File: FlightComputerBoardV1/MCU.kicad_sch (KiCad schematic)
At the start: 42 parts, among them J16 USB_C_Receptacle_USB2.0_16P, J17 Conn_ST_STDC14, SW1 SW_Push, SW2 SW_Push, U20 STM32H723ZGTx, X1 NX3215SA-32.768K-STD-MUA-9

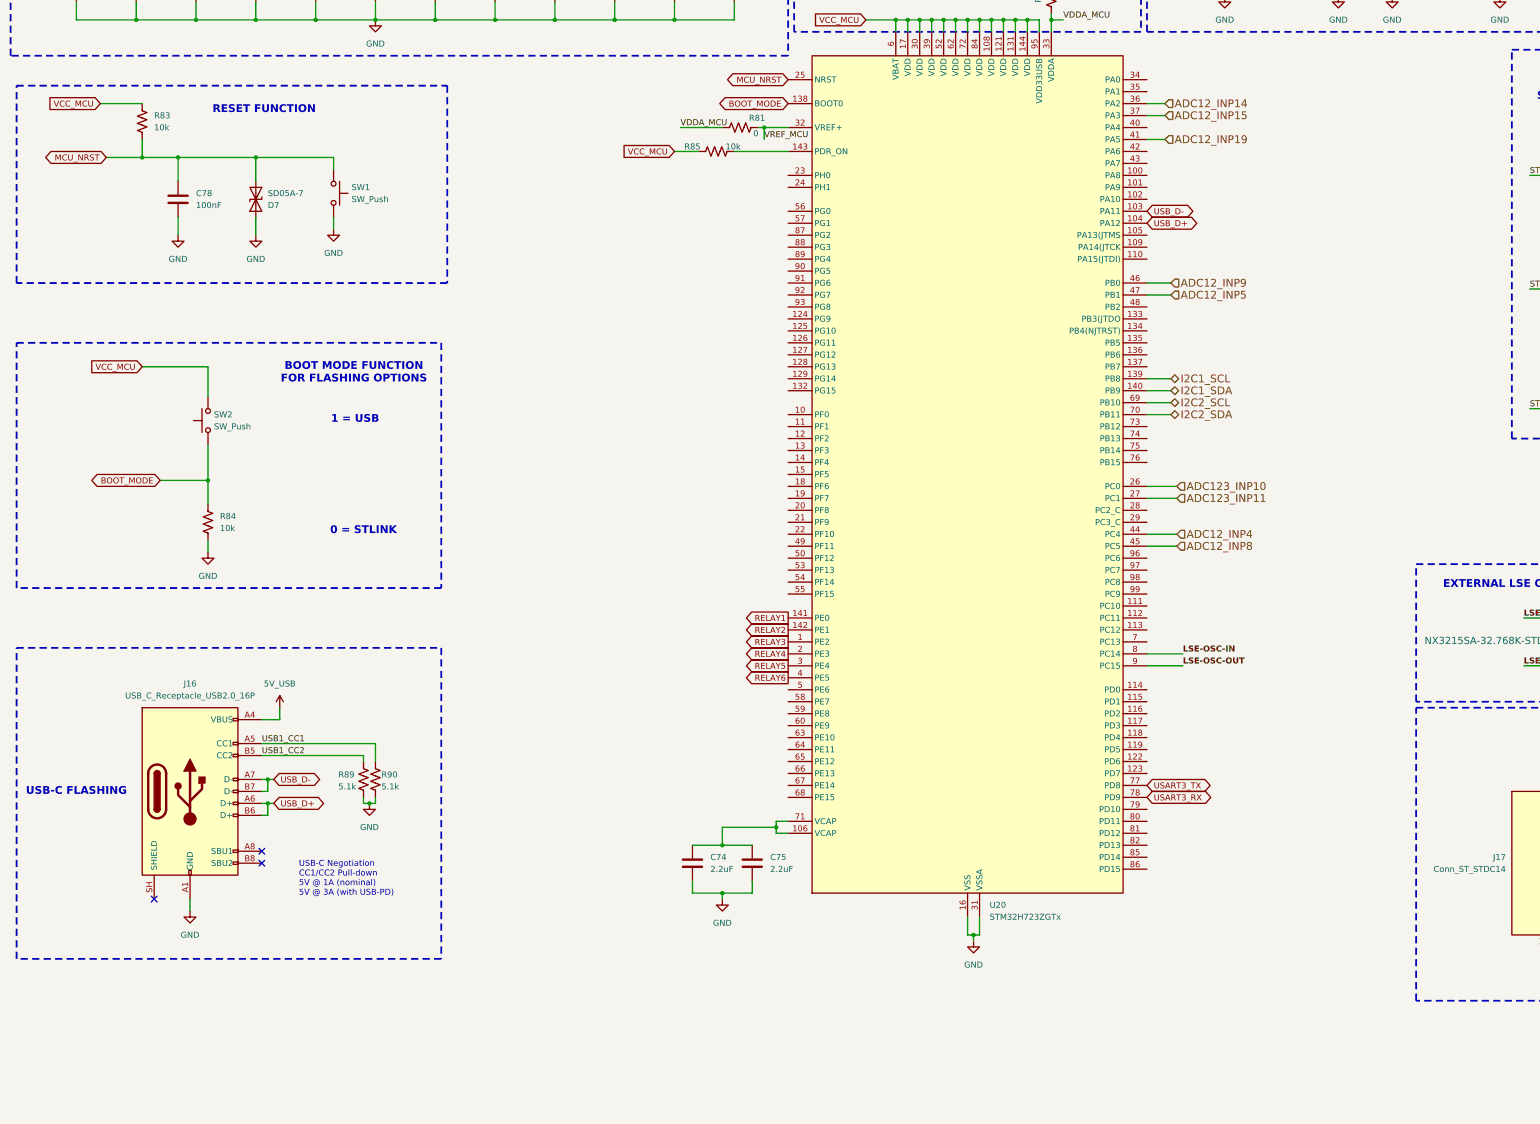
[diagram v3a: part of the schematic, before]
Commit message: Fixed I2C pull ups
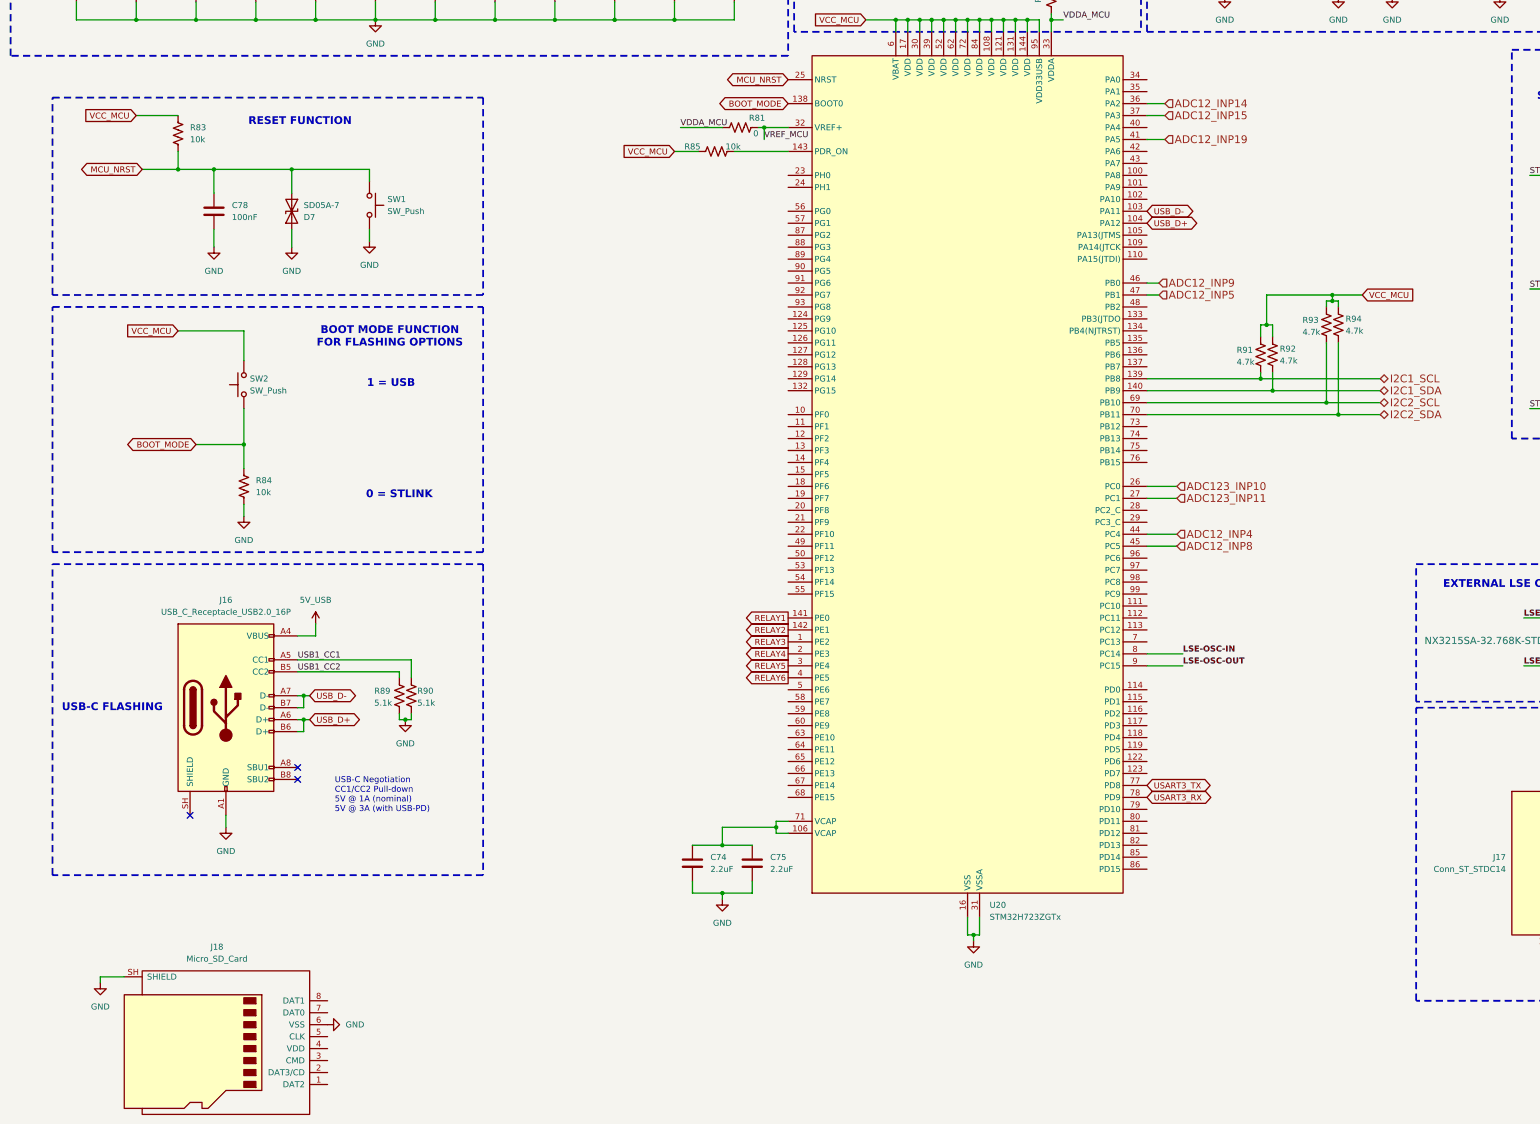
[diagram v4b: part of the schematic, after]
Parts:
- added J18: Micro_SD_Card, Connector_Card:microSD_HC_Wuerth_693072010801, symbol Connector:Micro_SD_Card
- added R91, R92, R93, R94: 4.7k, symbol Device:R_US
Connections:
- net +3V3: now also R91.1, R92.1, R93.1, R94.1
- net GND: now also J18.6 (VSS), J18.SH (SHIELD)
- net I2C1_SCL: now also R91.2
- net I2C1_SDA: now also R92.2
- net I2C2_SCL: now also R93.2
- net I2C2_SDA: now also R94.2
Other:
- moved on the sheet: C78, D7, J16, R83, R84, R89, R90, SW1, SW2

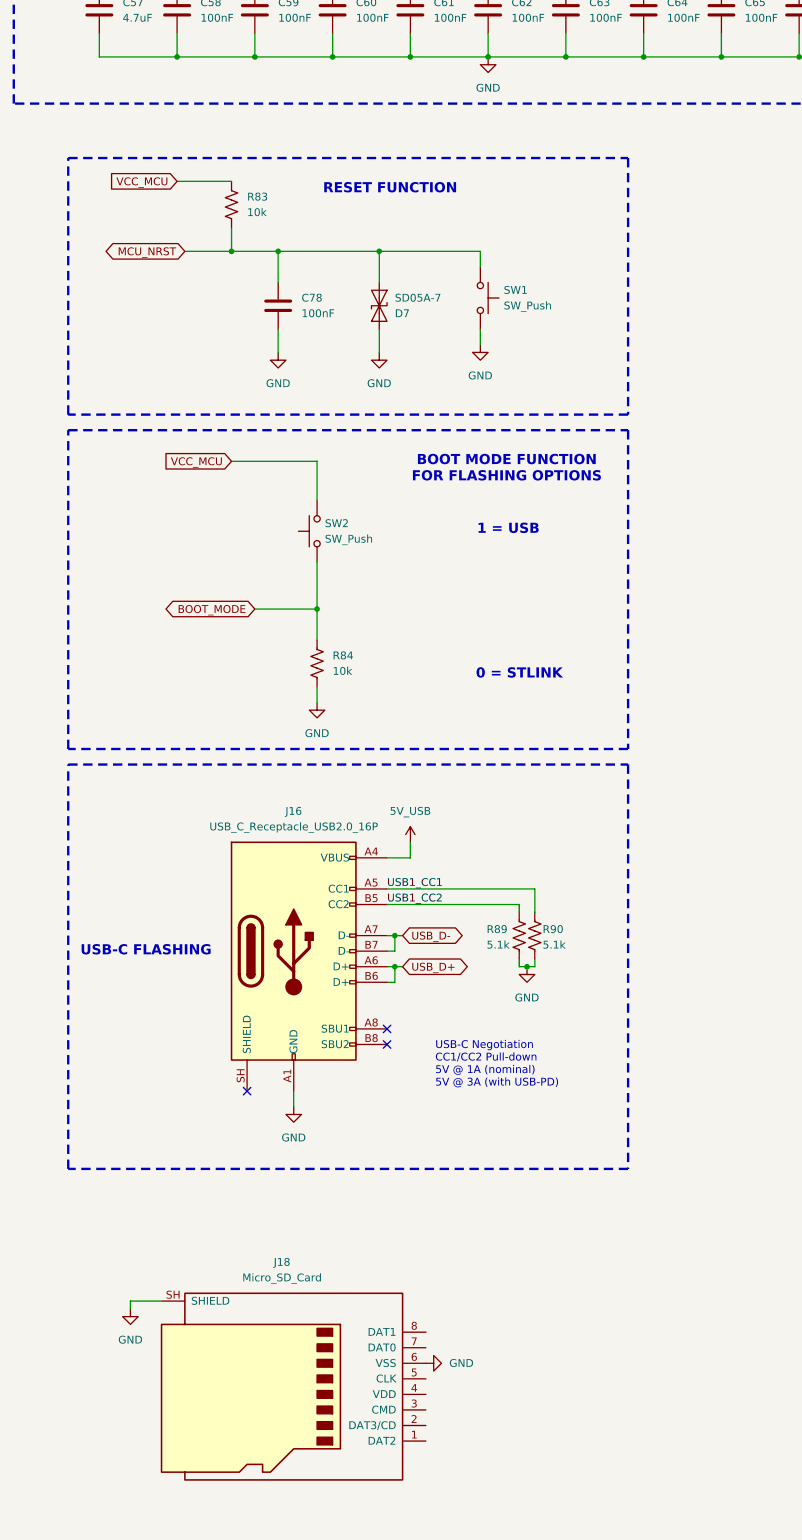
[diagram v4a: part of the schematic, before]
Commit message: added spi mode micro sd!
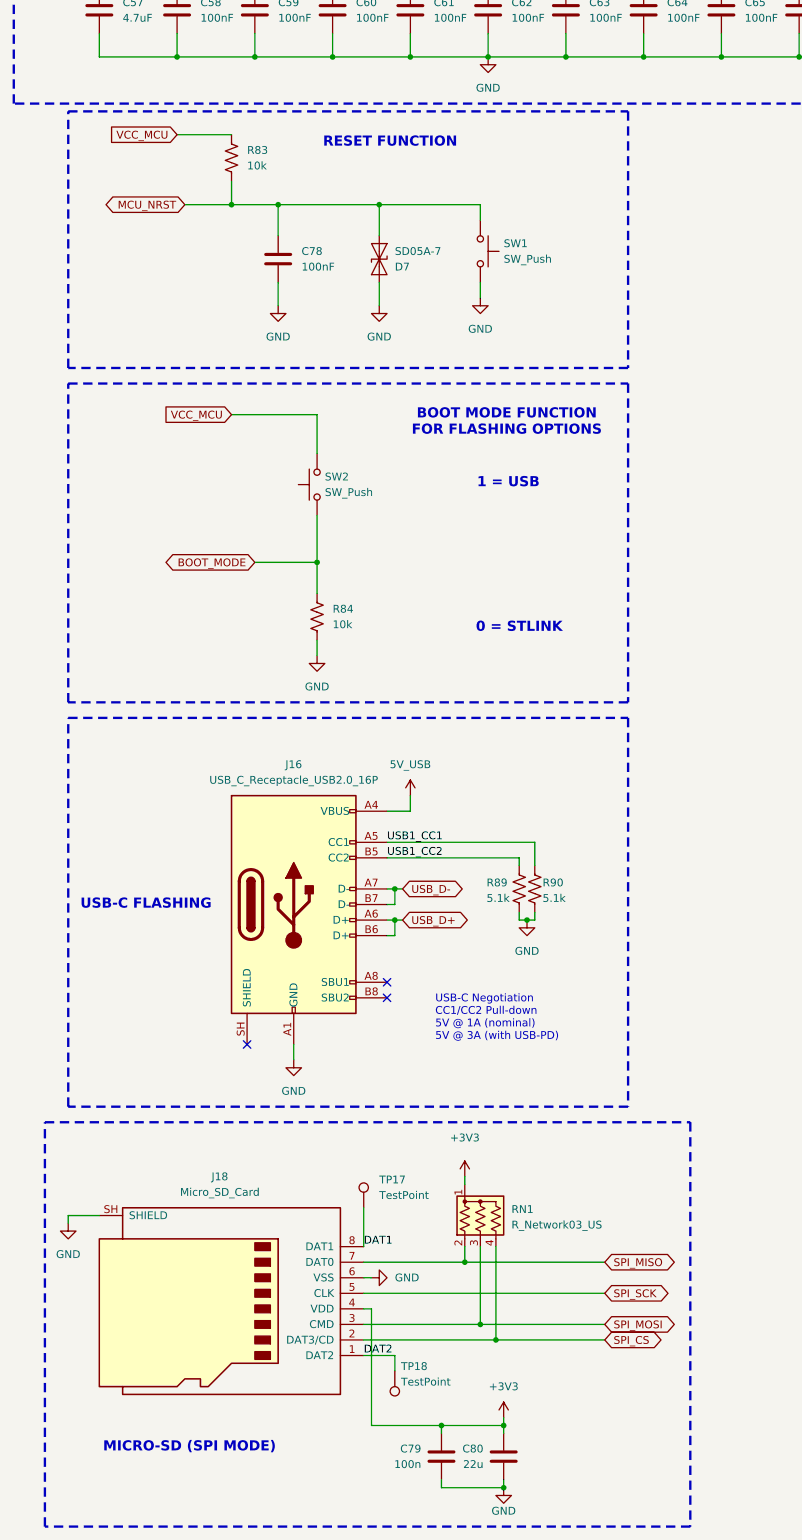
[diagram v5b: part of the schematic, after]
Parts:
- added C79: 100n, Capacitor_SMD:C_0402_1005Metric, symbol Device:C
- added C80: 22u, Capacitor_SMD:C_0805_2012Metric, symbol Device:C
- added RN1: R_Network03_US, Resistor_THT:R_Array_SIP4, symbol Device:R_Network03_US
- added TP17, TP18: TestPoint, Package_TO_SOT_SMD:SOT-23-5, symbol Connector:TestPoint
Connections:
- net +3V3: now also J18.4 (VDD), C79.1, C80.1, RN1.1 (common)
- net GND: now also C79.2, C80.2
- net DAT2: now reaches J18.1 (DAT2)
- net DAT2: now also TP18.1
- net SPI_CS: now reaches J18.2 (DAT3/CD)
- net SPI_CS: now also RN1.4 (R3)
- net SPI_MOSI: now reaches J18.3 (CMD)
- net SPI_MOSI: now also RN1.3 (R2)
- net SPI_SCK: now reaches J18.5 (CLK)
- net SPI_MISO: now reaches J18.7 (DAT0)
- net SPI_MISO: now also RN1.2 (R1)
- net DAT1: now reaches J18.8 (DAT1)
- net DAT1: now also TP17.1
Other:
- note added: "MICRO-SD (SPI MODE)"
- moved on the sheet: C78, D7, J16, J18, R83, R84, R89, R90, SW1, SW2

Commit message: minor clean up schematic
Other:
- note added: "STM32H723ZG FLIGHT COMPUTER"
- moved on the sheet: C78, C79, C80, D7, D8, J16, J18, R83, R84, R86, R89, R90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

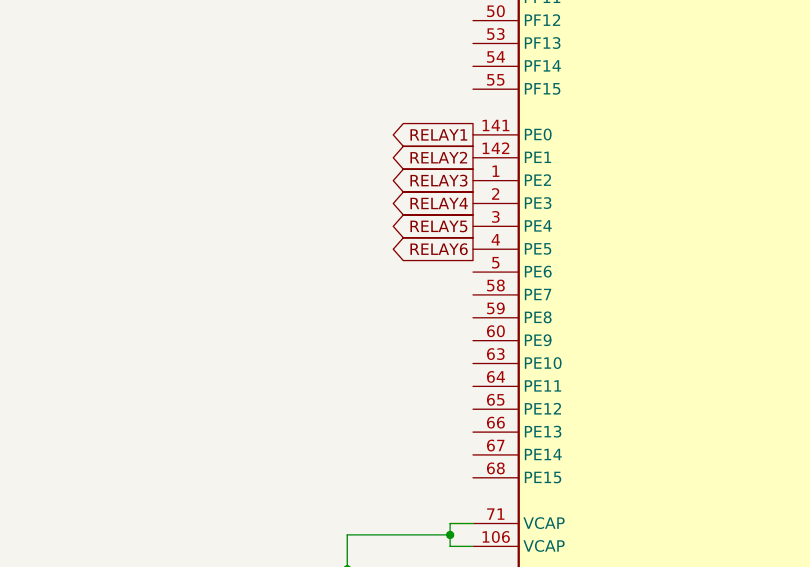
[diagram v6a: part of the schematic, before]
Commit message: Added 2 Linear Actuators
- Added symbols for ID10BT
- Added 2 ID10BTs to POWER sheet
- Added optocoupler and relay control circuit for ID10BTs
- Connected pins to MCU
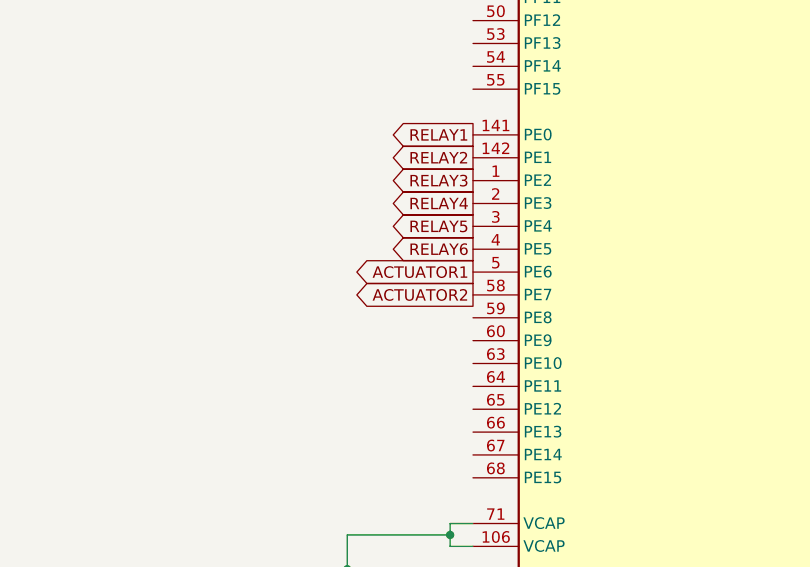
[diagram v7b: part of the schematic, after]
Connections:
- net ACTUATOR1: now reaches U20.5 (PE6)
- net ACTUATOR2: now reaches U20.58 (PE7)

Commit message: added HSE and ESD protection in MCU sheet
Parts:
- removed D7: SD05A-7, Diode_SMD:D_SOD-323_HandSoldering, symbol Diode:SD05C-01F
- added C94, C95: 10pF, XTAL_NX3215SA_NDK, symbol Device:C
- added R99: 0, Resistor_THT:R_Array_SIP4, symbol Device:R_US
- added U32: USBLC6-2SC6, Package_TO_SOT_SMD:SOT-23-6, symbol Power_Protection:USBLC6-2SC6
- added Y1: 25Mhz, C3E-25.000-12-3030-X-R:XTAL_C3E-25.000-12-3030-X-R, symbol C3E-25.000-12-3030-X-R:C3E-25.000-12-3030-X-R
- C76, C77: value 5.1pF -> 9.1pF
- X1: value NX3215SA-32.768K-STD-MUA-9 -> 32.768Khz
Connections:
- net 5V_USB: now also U32.5 (VBUS)
- net GND: now also C94.2, C95.2, U32.2 (GND), Y1.2 (GND), Y1.4 (GND)
- net STATUS_LED_1: now also D8.1 (K); no longer D8.2 (A)
- net STATUS_LED_2: now also D9.1 (K); no longer D9.2 (A)
- net STATUS_LED_3: now also D10.1 (K); no longer D10.2 (A)
- net SWCLK: now also U20.109 (PA14(JTCK)
- net SWDIO: now also U20.105 (PA13(JTMS)
- net USB1_CC1: now also R89.1; no longer R90.1
- net USB1_CC2: now also R90.1; no longer R89.1
- net USB_D+: now also U32.4 (I/O2); no longer J16.A6 (D+), J16.B6 (D+)
- net USB_D-: now also U32.6 (I/O1); no longer J16.A7 (D-), J16.B7 (D-)
- net at R87.2: now also D9.2 (A); no longer D9.1 (K)
- net at R88.2: now also D10.2 (A); no longer D10.1 (K)
- net at R86.2: now also D8.2 (A); no longer D8.1 (K)
- net HSE-OSC-IN: now reaches U20.23 (PH0)
- net HSE-OSC-IN: now also C95.1, Y1.3
- net at U20.24 (PH1): now also R99.2
- new net: J16.A7 (D-), J16.B7 (D-), U32.1 (I/O1)
- new net: J16.A6 (D+), J16.B6 (D+), U32.3 (I/O2)
- new net HSE-OSC-OUT: C94.1, R99.1, Y1.1
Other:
- moved on the sheet: C76, C77, D10, D8, D9, J17, X1
